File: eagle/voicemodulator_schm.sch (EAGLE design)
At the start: 27 parts, among them T1 2N5089, T2 2N5089, T3 2N5089, T4 2N5089

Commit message: Update schematic and rename folder
Folder has been renamed to "eagle" so that it's easier to find.
Schematic and PNG has been updated to a version that has no ERC errors.
Resistors and capacitor values still need to be assigned.
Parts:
- ATMEGA48A: value (none) -> uC; device atmel_tiny24-44-84tiny48-88mega48-88-168-328:ATMEGA48/88/168/328-PU(DIP28)PU -> ece411_fixes:ATMEGA48/88/168/328-PU(DIP28)PU
- DAC: value MCP4921-E/MS -> MCP4921-E/P; device dac:MCP4921-E/MS -> Microchip_By_element14_Batch_1:MCP4921-E/P
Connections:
- net 0: now also ATMEGA48A.AREF, ATMEGA48A.GND0, ATMEGA48A.GND1, DAC.AVSS, DAC.~LDAC; no longer ATMEGA48AIC.AREF, DACA.LDAC
- net N$16: now also ATMEGA48A.PB3(MOSI/OC2A/PCINT3), DAC.SDI; no longer ATMEGA48AIC.PB3(MOSI/OC2A/PCINT3), DACA.SDI
- net N$17: now also ATMEGA48A.PB5(SCK/PCINT5), DAC.SCK; no longer ATMEGA48AIC.PB5(SCK/PCINT5), DACA.SCK
- net N$19: now also ATMEGA48A.PD7(AIN1/PCINT23); no longer ATMEGA48AIC.PD7(AIN1/PCINT23)
- net N$2: now also ATMEGA48A.PB4(MISO/PCINT4); no longer ATMEGA48AIC.PB4(MISO/PCINT4)
- net N$20: now also ATMEGA48A.PB6(XTAL1/TOSC1/PCINT6), DAC.~CS; no longer ATMEGA48AIC.PB6(XTAL1/TOSC1/PCINT6), DACA.CS
- net N$22: now also ATMEGA48A.PC6(!RESET!/PCINT14); no longer ATMEGA48AIC.PC6(!RESET!/PCINT14)
- net N$4: now also DAC.VOUTA; no longer DACA.VOUT
- net VCC: now also ATMEGA48A.AVCC, ATMEGA48A.VCC, DAC.VDD, DAC.VREFA; no longer ATMEGA48AIC.AVCC, DACA.VREF
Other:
- note added: "ISP Programming"

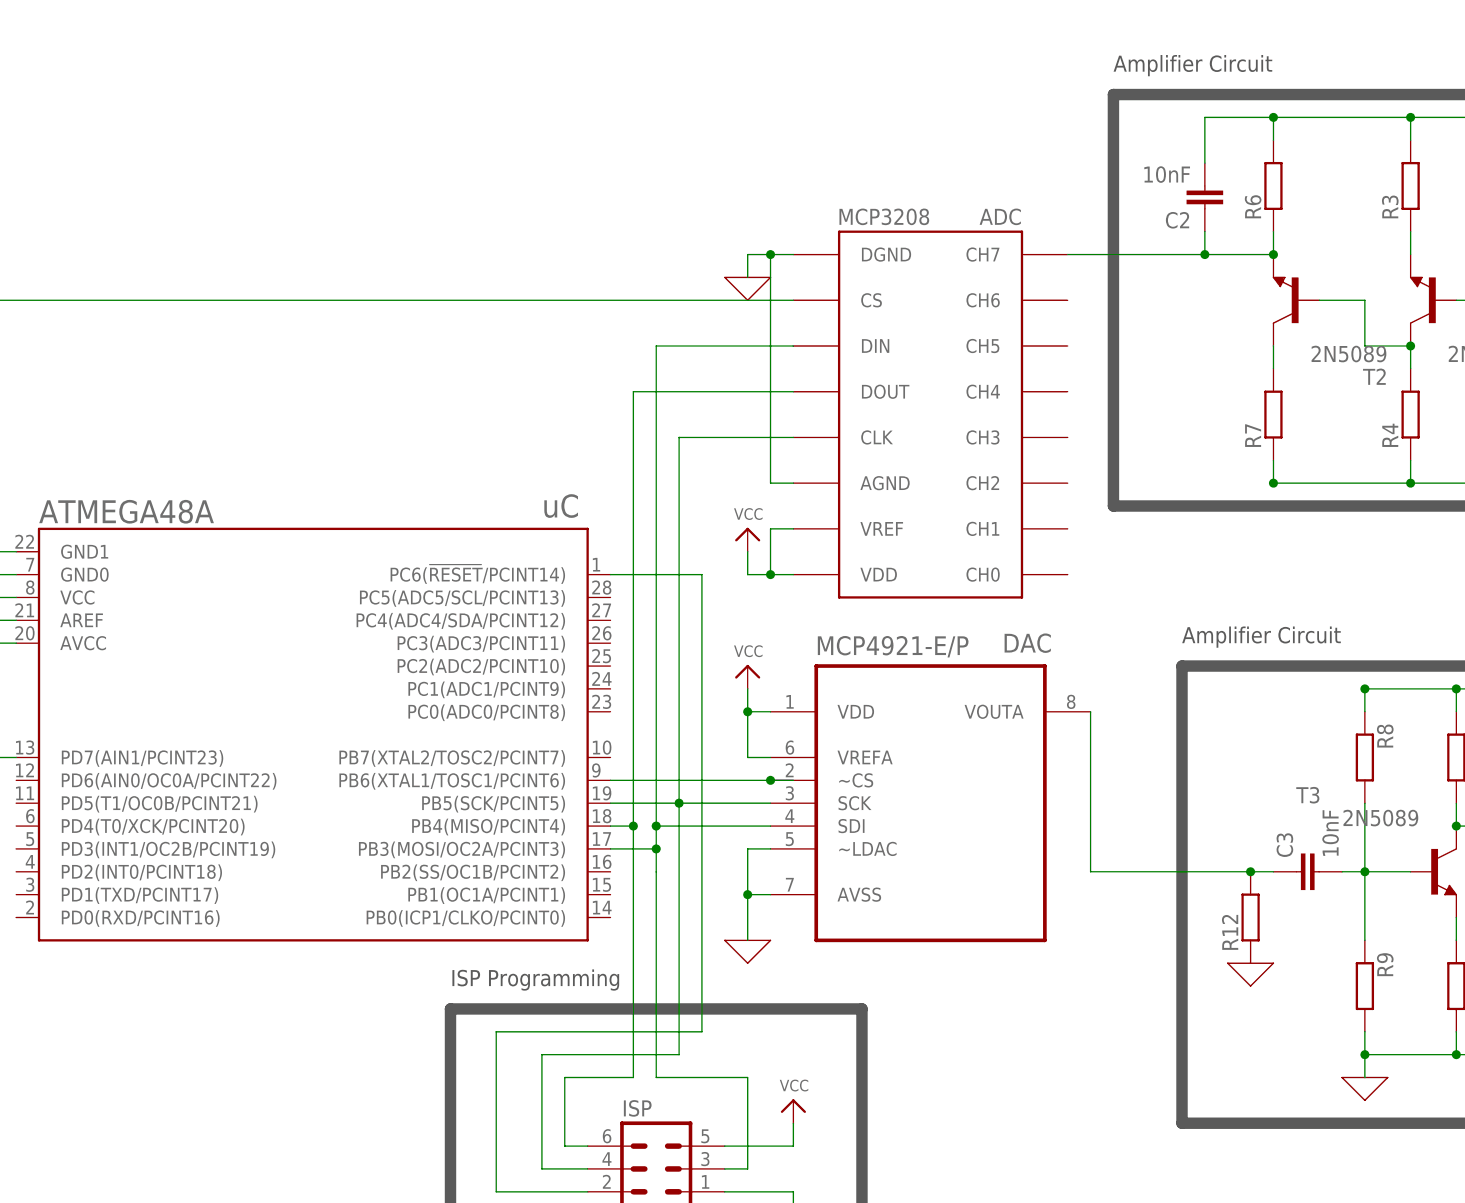
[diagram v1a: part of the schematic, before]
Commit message: Pullup resistor added, testpoints at ADC in and DAC out added.
Pictures, board layout and schematic all updated.
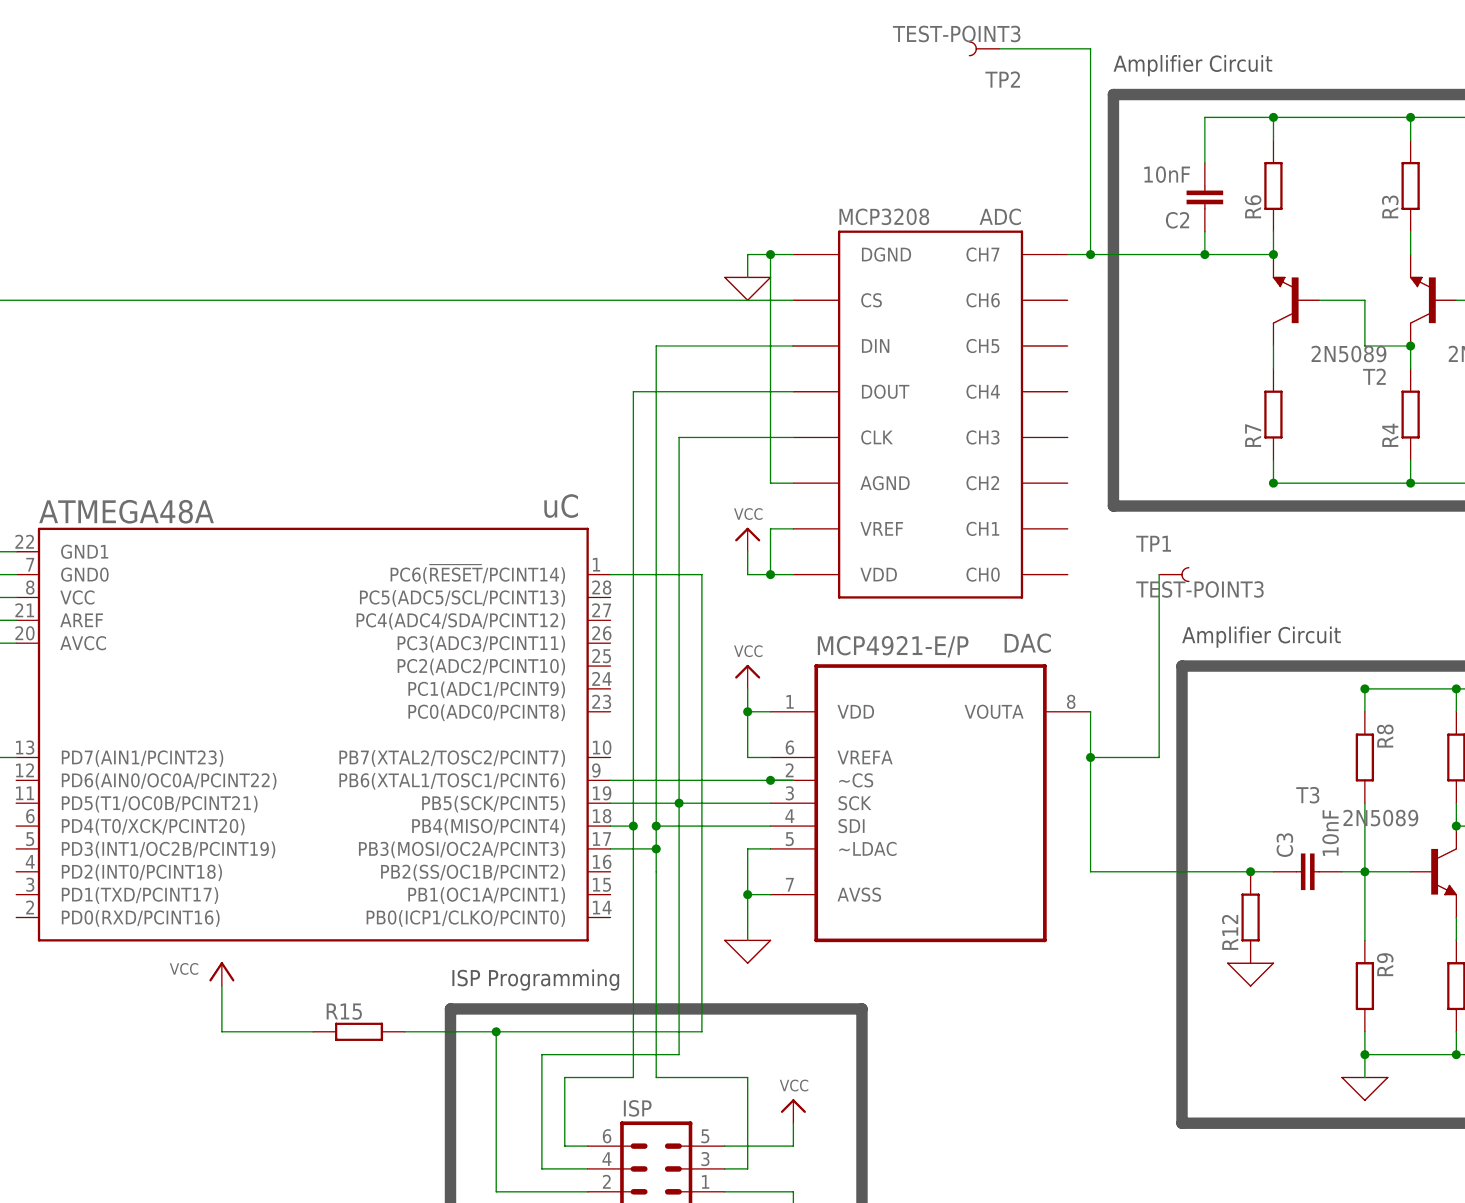
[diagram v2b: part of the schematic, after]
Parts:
- added R15: (no value), resistor-shunt:SMR-WAV
- added TP1, TP2: TEST-POINT3, SparkFun-Connectors:TEST-POINT3
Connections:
- net N$22: now also R15.1
- net N$4: now also TP1.1
- net N$5: now also TP2.1
- net VCC: now also R15.2

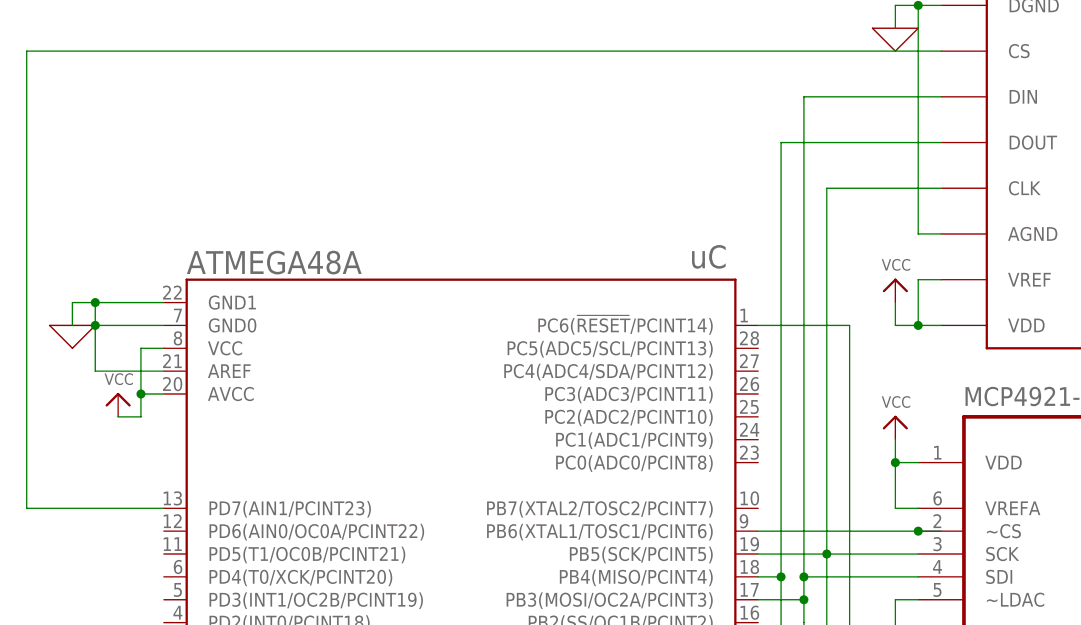
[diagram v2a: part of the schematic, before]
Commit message: Added 10 mm Power LEDs
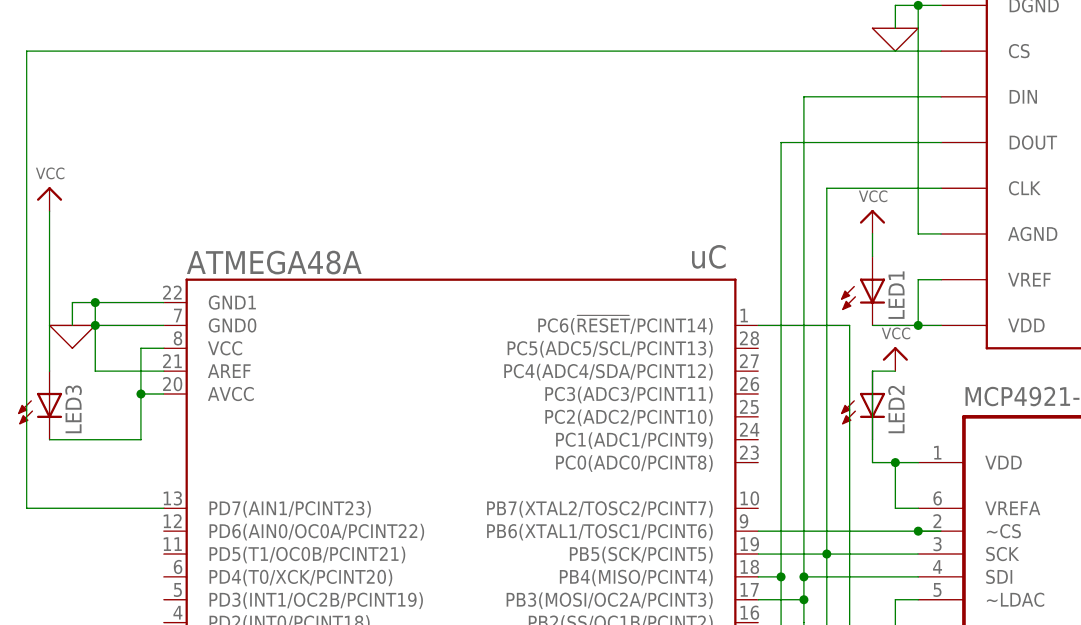
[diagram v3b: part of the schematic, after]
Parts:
- added LED1, LED2, LED3: (no value), led:LED10MM
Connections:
- new net N$18: ADC.VDD, ADC.VREF, LED1.C
- new net N$21: ATMEGA48A.AVCC, ATMEGA48A.VCC, LED3.C
- net VCC: now also LED1.A, LED2.A, LED2.C, LED3.A; no longer ADC.VDD, ADC.VREF, ATMEGA48A.AVCC, ATMEGA48A.VCC
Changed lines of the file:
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@@
 <part name="P+3" library="supply1" library_urn="urn:adsk.eagle:library:371" deviceset="VCC" device=""/>
 <part name="R15" library="resistor-shunt" library_urn="urn:adsk.eagle:library:346" deviceset="SMR-WAV" device="" package3d_urn="urn:adsk.eagle:package:25223/1"/>
+<part name="LED1" library="led" library_urn="urn:adsk.eagle:library:259" deviceset="LED" device="10MM" package3d_urn="urn:adsk.eagle:package:15828/1"/>
+<part name="LED2" library="led" library_urn="urn:adsk.eagle:library:259" deviceset="LED" device="10MM" package3d_urn="urn:adsk.eagle:package:15828/1"/>
+<part name="LED3" library="led" library_urn="urn:adsk.eagle:library:259" deviceset="LED" device="10MM" package3d_urn="urn:adsk.eagle:package:15828/1"/>
 </parts>
 <sheets>
@@
 <instance part="X_1" gate="G$1" x="165.1" y="63.5"/>
 <instance part="X_2" gate="G$1" x="48.26" y="2.54"/>
-<instance part="P+1" gate="VCC" x="48.26" y="33.02">
-<attribute name="VALUE" x="46.736" y="34.036" size="1.27" layer="96"/>
+<instance part="P+1" gate="VCC" x="48.26" y="40.64">
+<attribute name="VALUE" x="46.736" y="41.656" size="1.27" layer="96"/>
 </instance>
 <instance part="R1" gate="G$1" x="132.08" y="60.96" rot="R90">
@@
 <instance part="X_7" gate="G$1" x="116.84" y="-12.7"/>
 <instance part="X_8" gate="G$1" x="48.26" y="76.2"/>
-<instance part="P+2" gate="VCC" x="48.26" y="48.26">
-<attribute name="VALUE" x="46.736" y="49.276" size="1.27" layer="96"/>
+<instance part="P+2" gate="VCC" x="45.72" y="55.88">
+<attribute name="VALUE" x="44.196" y="56.896" size="1.27" layer="96"/>
 </instance>
 <instance part="X_9" gate="G$1" x="-43.18" y="43.18"/>
@@
 <attribute name="VALUE" x="128.016" y="67.056" size="1.27" layer="96"/>
 </instance>
-<instance part="P+5" gate="VCC" x="-38.1" y="35.56">
-<attribute name="VALUE" x="-39.624" y="36.576" size="1.27" layer="96"/>
+<instance part="P+5" gate="VCC" x="-45.72" y="58.42">
+<attribute name="VALUE" x="-47.244" y="59.436" size="1.27" layer="96"/>
 </instance>
 <instance part="ISP" gate="1" x="38.1" y="-22.86">
@@
 <attribute name="NAME" x="1.27" y="-6.2484" size="1.778" layer="95"/>
 <attribute name="VALUE" x="1.27" y="-10.541" size="1.778" layer="96"/>
+</instance>
+<instance part="LED1" gate="G$1" x="45.72" y="48.26">
+<attribute name="NAME" x="49.276" y="43.688" size="1.778" layer="95" rot="R90"/>
+<attribute name="VALUE" x="51.435" y="43.688" size="1.778" layer="96" rot="R90"/>
+</instance>
+<instance part="LED2" gate="G$1" x="45.72" y="35.56">
+<attribute name="NAME" x="49.276" y="30.988" size="1.778" layer="95" rot="R90"/>
+<attribute name="VALUE" x="51.435" y="30.988" size="1.778" layer="96" rot="R90"/>
+</instance>
+<instance part="LED3" gate="G$1" x="-45.72" y="35.56">
+<attribute name="NAME" x="-42.164" y="30.988" size="1.778" layer="95" rot="R90"/>
+<attribute name="VALUE" x="-40.005" y="30.988" size="1.778" layer="96" rot="R90"/>
 </instance>
 </instances>
@@
 <net name="VCC" class="0">
 <segment>
-<pinref part="P+2" gate="VCC" pin="VCC"/>
-<wire x1="48.26" y1="45.72" x2="48.26" y2="43.18" width="0.127" layer="91"/>
-<pinref part="ADC" gate="G$1" pin="VREF"/>
-<wire x1="53.34" y1="48.26" x2="50.8" y2="48.26" width="0.127" layer="91"/>
-<wire x1="50.8" y1="48.26" x2="50.8" y2="43.18" width="0.127" layer="91"/>
-<pinref part="ADC" gate="G$1" pin="VDD"/>
-<wire x1="50.8" y1="43.18" x2="53.34" y2="43.18" width="0.127" layer="91"/>
-<wire x1="48.26" y1="43.18" x2="50.8" y2="43.18" width="0.127" layer="91"/>
-<junction x="50.8" y="43.18"/>
-</segment>
-<segment>
 <pinref part="ISP" gate="1" pin="5"/>
 <wire x1="45.72" y1="-20.32" x2="53.34" y2="-20.32" width="0.1524" layer="91"/>
@@
 </segment>
 <segment>
-<pinref part="ATMEGA48A" gate="IC" pin="VCC"/>
-<wire x1="-33.02" y1="40.64" x2="-35.56" y2="40.64" width="0.1524" layer="91"/>
-<wire x1="-35.56" y1="40.64" x2="-35.56" y2="35.56" width="0.1524" layer="91"/>
-<pinref part="P+5" gate="VCC" pin="VCC"/>
-<wire x1="-35.56" y1="35.56" x2="-35.56" y2="33.02" width="0.1524" layer="91"/>
-<wire x1="-35.56" y1="33.02" x2="-38.1" y2="33.02" width="0.1524" layer="91"/>
-<pinref part="ATMEGA48A" gate="IC" pin="AVCC"/>
-<wire x1="-33.02" y1="35.56" x2="-35.56" y2="35.56" width="0.1524" layer="91"/>
-<junction x="-35.56" y="35.56"/>
-</segment>
-<segment>
-<pinref part="DAC" gate="A" pin="VDD"/>
-<wire x1="50.8" y1="27.94" x2="48.26" y2="27.94" width="0.1524" layer="91"/>
-<pinref part="P+1" gate="VCC" pin="VCC"/>
-<wire x1="48.26" y1="27.94" x2="48.26" y2="30.48" width="0.1524" layer="91"/>
-<pinref part="DAC" gate="A" pin="VREFA"/>
-<wire x1="50.8" y1="22.86" x2="48.26" y2="22.86" width="0.1524" layer="91"/>
-<wire x1="48.26" y1="22.86" x2="48.26" y2="27.94" width="0.1524" layer="91"/>
-<junction x="48.26" y="27.94"/>
-</segment>
-<segment>
 <wire x1="-10.16" y1="-7.62" x2="-10.16" y2="-2.54" width="0.1524" layer="91"/>
 <pinref part="P+3" gate="VCC" pin="VCC"/>
 <pinref part="R15" gate="G$1" pin="2"/>
 <wire x1="0" y1="-7.62" x2="-10.16" y2="-7.62" width="0.1524" layer="91"/>
+</segment>
+<segment>
+<pinref part="LED1" gate="G$1" pin="A"/>
+<pinref part="P+2" gate="VCC" pin="VCC"/>
+<wire x1="45.72" y1="50.8" x2="45.72" y2="53.34" width="0.1524" layer="91"/>
+</segment>
+<segment>
+<pinref part="P+1" gate="VCC" pin="VCC"/>
+<pinref part="LED2" gate="G$1" pin="A"/>
+<wire x1="48.26" y1="38.1" x2="45.72" y2="38.1" width="0.1524" layer="91"/>
+<pinref part="LED2" gate="G$1" pin="C"/>
+<wire x1="45.72" y1="38.1" x2="45.72" y2="30.48" width="0.1524" layer="91"/>
+<pinref part="DAC" gate="A" pin="VDD"/>
+<wire x1="50.8" y1="27.94" x2="48.26" y2="27.94" width="0.1524" layer="91"/>
+<pinref part="DAC" gate="A" pin="VREFA"/>
+<wire x1="50.8" y1="22.86" x2="48.26" y2="22.86" width="0.1524" layer="91"/>
+<wire x1="48.26" y1="22.86" x2="48.26" y2="27.94" width="0.1524" layer="91"/>
+<wire x1="45.72" y1="30.48" x2="45.72" y2="27.94" width="0.1524" layer="91"/>
+<wire x1="45.72" y1="27.94" x2="48.26" y2="27.94" width="0.1524" layer="91"/>
+<junction x="48.26" y="27.94"/>
+</segment>
+<segment>
+<pinref part="LED3" gate="G$1" pin="A"/>
+<pinref part="P+5" gate="VCC" pin="VCC"/>
+<wire x1="-45.72" y1="38.1" x2="-45.72" y2="55.88" width="0.1524" layer="91"/>
 </segment>
 </net>
@@
 </segment>
 </net>
+<net name="N$18" class="0">
+<segment>
+<pinref part="ADC" gate="G$1" pin="VREF"/>
+<wire x1="53.34" y1="48.26" x2="50.8" y2="48.26" width="0.127" layer="91"/>
+<wire x1="50.8" y1="48.26" x2="50.8" y2="43.18" width="0.127" layer="91"/>
+<pinref part="ADC" gate="G$1" pin="VDD"/>
+<wire x1="50.8" y1="43.18" x2="53.34" y2="43.18" width="0.127" layer="91"/>
+<wire x1="48.26" y1="43.18" x2="50.8" y2="43.18" width="0.127" layer="91"/>
+<junction x="50.8" y="43.18"/>
+<pinref part="LED1" gate="G$1" pin="C"/>
+<wire x1="45.72" y1="43.18" x2="48.26" y2="43.18" width="0.1524" layer="91"/>
+</segment>
+</net>
+<net name="N$21" class="0">
+<segment>
+<pinref part="ATMEGA48A" gate="IC" pin="VCC"/>
+<wire x1="-33.02" y1="40.64" x2="-35.56" y2="40.64" width="0.1524" layer="91"/>
+<wire x1="-35.56" y1="40.64" x2="-35.56" y2="35.56" width="0.1524" layer="91"/>
+<pinref part="ATMEGA48A" gate="IC" pin="AVCC"/>
+<wire x1="-33.02" y1="35.56" x2="-35.56" y2="35.56" width="0.1524" layer="91"/>
+<junction x="-35.56" y="35.56"/>
+<pinref part="LED3" gate="G$1" pin="C"/>
+<wire x1="-45.72" y1="30.48" x2="-35.56" y2="30.48" width="0.1524" layer="91"/>
+<wire x1="-35.56" y1="30.48" x2="-35.56" y2="35.56" width="0.1524" layer="91"/>
+</segment>
+</net>
